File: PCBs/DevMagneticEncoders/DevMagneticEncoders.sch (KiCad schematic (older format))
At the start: 23 parts, among them J1 Conn_01x06_Male, J2 Conn_01x06_Male, J3 Screw_Terminal_01x02, J4 Conn_02x03_Odd_Even, J5 Conn_02x03_Odd_Even, J6 Conn_01x06_Male, J7 Conn_01x04_Male, J8 Conn_01x04_Male, U1 AZ1117-3.3, U2 ESP32-S2-WROOM

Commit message: 5 stepper board
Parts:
- removed J6: Conn_01x06_Male, Connector_JST:JST_PH_B6B-PH-K_1x06_P2.00mm_Vertical, symbol Connector:Conn_01x06_Male
- added A3, A4, A5: Pololu_Breakout_DRV8825, Module:Pololu_Breakout-16_15.2x20.3mm, symbol Driver_Motor:Pololu_Breakout_DRV8825
- added C10: 0.1U, Capacitor_SMD:C_0805_2012Metric_Pad1.18x1.45mm_HandSolder, symbol Device:C
- added C11: 100U, Capacitor_SMD:CP_Elec_6.3x7.7, symbol Device:CP
- added C12, C13, C14: 100u, Capacitor_SMD:CP_Elec_6.3x7.7, symbol Device:CP
- added C15, C16, C17, C7, C8: 0.1u, Capacitor_SMD:C_0805_2012Metric_Pad1.18x1.45mm_HandSolder, symbol Device:C
- added C9: 1U, Capacitor_SMD:C_0805_2012Metric_Pad1.18x1.45mm_HandSolder, symbol Device:C
- added J10, J11, J12: Conn_01x06_Male, Connector_JST:JST_XH_B6B-XH-A_1x06_P2.50mm_Vertical, symbol Connector:Conn_01x06_Male
- added J13, J14, J15: Conn_02x03_Odd_Even, Connector_PinHeader_2.54mm:PinHeader_2x03_P2.54mm_Vertical, symbol Connector_Generic:Conn_02x03_Odd_Even
- added J16, J17, J18: Conn_01x04_Male, Connector_JST:JST_XH_B4B-XH-A_1x04_P2.50mm_Vertical, symbol Connector:Conn_01x04_Male
- added J6: Conn_01x03_Male, Connector_PinHeader_2.54mm:PinHeader_1x03_P2.54mm_Vertical, symbol Connector:Conn_01x03_Male
- added J9: Conn_01x02_Male, Connector_JST:JST_XH_B2B-XH-A_1x02_P2.50mm_Vertical, symbol Connector:Conn_01x02_Male
- added R5: 0.1, Resistor_SMD:R_0805_2012Metric_Pad1.20x1.40mm_HandSolder, symbol Device:R
- added S2: TL3315NF160Q, A4:TL3305AF160QG, symbol dk_Tactile-Switches:TL3315NF160Q
- added U3: ZXBM5210-S, Package_SO:SOIC-8_3.9x4.9mm_P1.27mm, symbol Driver_Motor:ZXBM5210-S
- added U4: TB67H451FNG,EL, Package_SO:SOIC-8-1EP_3.9x4.9mm_P1.27mm_EP2.29x3mm_ThermalVias, symbol BoilerBot:TB67H451FNG,EL
- S1: footprint A4:CK_PTS647_4.5x4.5 -> A4:TL3305AF160QG
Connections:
- net +12V: now also A3.8 (VMOT), A4.8 (VMOT), A5.8 (VMOT), C10.1, C11.1, C12.1, C13.1, C14.1, C15.1, C16.1, C17.1, C7.1, C8.1, U3.2 (VM), U4.5 (VM)
- net +3V3: now also A3.13 (~RST), A3.14 (~SLP), A4.13 (~RST), A4.14 (~SLP), A5.13 (~RST), A5.14 (~SLP), C9.1, J10.1 (Pin_1), J11.1 (Pin_1), J12.1 (Pin_1), J13.1 (Pin_1), J13.3 (Pin_3), J13.5 (Pin_5), J14.1 (Pin_1), J14.3 (Pin_3), J14.5 (Pin_5), J15.1 (Pin_1), J15.3 (Pin_3), J15.5 (Pin_5), U3.3 (VDD)
- net CHARGE: now also U2.16 (IO13); no longer U2.20 (IO17)
- net CLK: now also U2.29 (IO35), J10.3 (Pin_3), J11.3 (Pin_3), J12.3 (Pin_3); no longer U2.25 (IO26)
- net CS0: now also U2.39 (IO45); no longer U2.27 (IO33)
- net CS1: now also U2.36 (IO42); no longer U2.23 (IO20)
- net EN1: now also U2.15 (IO12); no longer U2.6 (IO3)
- net GND: now also A3.1 (GND), A3.7 (GND), A4.1 (GND), A4.7 (GND), A5.1 (GND), A5.7 (GND), C10.2, C11.2, C12.2, C13.2, C14.2, C15.2, C16.2, C17.2, C7.2, C8.2, C9.2, J10.2 (Pin_2), J11.2 (Pin_2), J12.2 (Pin_2), J6.3 (Pin_3), R5.2, S2.4, U3.8 (GND), U4.1 (GND), U4.9 (EP)
- net IO0: now also S2.1
- net MISO: now also U2.34 (IO40), J10.4 (Pin_4), J11.4 (Pin_4), J12.4 (Pin_4); no longer U2.24 (IO21)
- net MOSI: now also U2.31 (IO37), J10.6 (Pin_6), J11.6 (Pin_6), J12.6 (Pin_6); no longer U2.22 (IO19)
- net RX: now also J6.2 (Pin_2)
- net TX: now also J6.1 (Pin_1)
- net EN3: now reaches U2.11 (IO8)
- net EN3: now also A4.9 (~EN)
- net DIR2: now reaches U2.12 (IO9)
- net DIR2: now also A3.16 (DIR)
- net STEP2: now reaches U2.13 (IO10)
- net STEP2: now also A3.15 (STEP)
- net EN2: now reaches U2.14 (IO11)
- net EN2: now also A3.9 (~EN)
- net CS4: now reaches U2.28 (IO34)
- net CS4: now also J12.5 (Pin_5)
- net CS3: now reaches U2.30 (IO36)
- net CS3: now also J11.5 (Pin_5)
- net MOT1: now reaches U2.32 (IO38)
- net MOT1: now also U3.4 (FWD), U4.3 (IN1)
- net MOT2: now reaches U2.33 (IO39)
- net MOT2: now also U3.5 (REV), U4.2 (IN2)
- net CS2: now reaches U2.35 (IO41)
- net CS2: now also J10.5 (Pin_5)
- new net: A5.12 (M2), J15.2 (Pin_2)
- new net: A5.11 (M1), J15.4 (Pin_4)
- new net: A5.10 (M0), J15.6 (Pin_6)
- new net: A5.6 (B2), J18.1 (Pin_1)
- new net: A5.5 (B1), J18.2 (Pin_2)
- new net: A5.4 (A1), J18.3 (Pin_3)
- new net: A5.3 (A2), J18.4 (Pin_4)
- new net: A4.12 (M2), J14.2 (Pin_2)
- new net: A4.11 (M1), J14.4 (Pin_4)
- new net: A4.10 (M0), J14.6 (Pin_6)
- new net: A4.6 (B2), J17.1 (Pin_1)
- new net: A4.5 (B1), J17.2 (Pin_2)
- new net: A4.4 (A1), J17.3 (Pin_3)
- new net: A4.3 (A2), J17.4 (Pin_4)
- new net: A3.12 (M2), J13.2 (Pin_2)
- new net: A3.11 (M1), J13.4 (Pin_4)
- new net: A3.10 (M0), J13.6 (Pin_6)
- new net: A3.6 (B2), J16.1 (Pin_1)
- new net: A3.5 (B1), J16.2 (Pin_2)
- new net: A3.4 (A1), J16.3 (Pin_3)
- new net: A3.3 (A2), J16.4 (Pin_4)
- new net DAC1: U2.20 (IO17), U3.6 (VREF), U4.4 (VREF)
- new net DIR3: A4.16 (DIR), U2.23 (IO20)
- new net DIR4: A5.16 (DIR), U2.27 (IO33)
- new net EN4: A5.9 (~EN), U2.24 (IO21)
- new net OUT1: J9.2 (Pin_2), U3.1 (OUT1), U4.6 (OUT1)
- new net OUT2: J9.1 (Pin_1), U3.7 (OUT2), U4.8 (OUT2)
- new net RS: R5.1, U4.7 (RS)
- new net STEP3: A4.15 (STEP), U2.22 (IO19)
- new net STEP4: A5.15 (STEP), U2.25 (IO26)
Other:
- moved on the sheet: C6, R3, R4

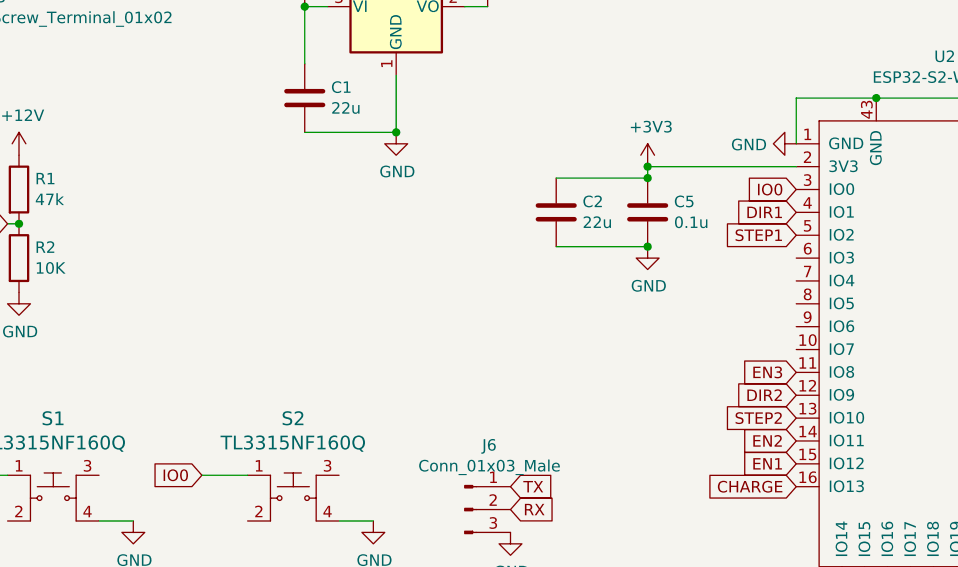
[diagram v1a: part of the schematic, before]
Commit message: added load cell connector
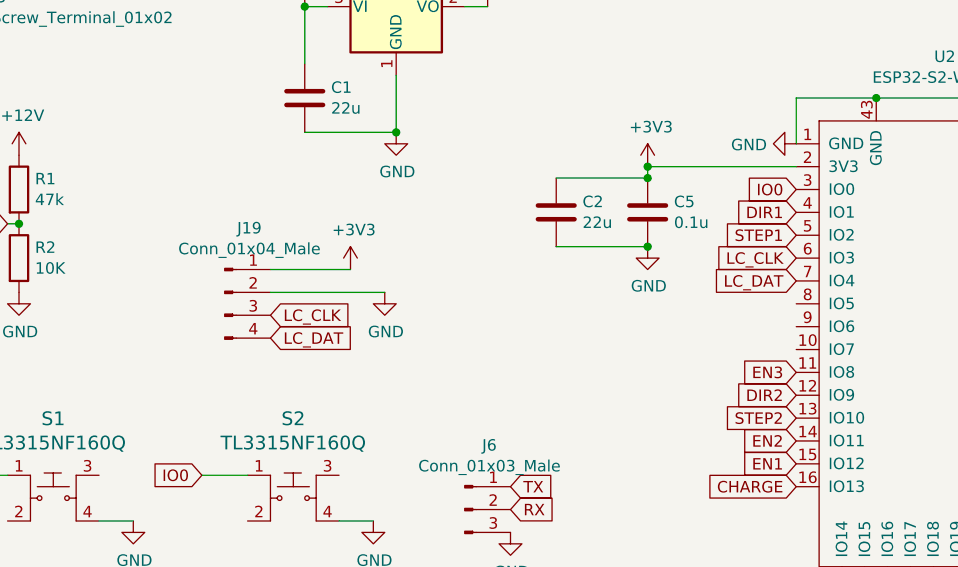
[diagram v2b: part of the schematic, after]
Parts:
- added J19: Conn_01x04_Male, Connector_JST:JST_XH_B4B-XH-A_1x04_P2.50mm_Vertical, symbol Connector:Conn_01x04_Male
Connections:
- net +3V3: now also J19.1 (Pin_1)
- net GND: now also J19.2 (Pin_2)
- net LC_CLK: now reaches U2.6 (IO3)
- net LC_CLK: now also J19.3 (Pin_3)
- net LC_DAT: now reaches U2.7 (IO4)
- net LC_DAT: now also J19.4 (Pin_4)
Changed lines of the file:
@@
 Wire Wire Line
 	6200 1800 6550 1800
+$Comp
+L Connector:Conn_01x04_Male J19
+U 1 1 6113B222
+P 2400 2350
+AR Path="/6113B222" Ref="J19"  Part="1"
+AR Path="/6090A275/6113B222" Ref="J?"  Part="1"
+AR Path="/60A3186D/6090A275/6113B222" Ref="J?"  Part="1"
+F 0 "J19" H 2508 2631 50  0000 C CNN
+F 1 "Conn_01x04_Male" H 2508 2540 50  0000 C CNN
+F 2 "Connector_JST:JST_XH_B4B-XH-A_1x04_P2.50mm_Vertical" H 2400 2350 50  0001 C CNN
+F 3 "~" H 2400 2350 50  0001 C CNN
+	1    2400 2350
+	1    0    0    -1
+$EndComp
+$Comp
+L power:+3V3 #PWR?
+U 1 1 6113C85F
+P 2950 2250
+AR Path="/60A3186D/6113C85F" Ref="#PWR?"  Part="1"
+AR Path="/6113C85F" Ref="#PWR060"  Part="1"
+F 0 "#PWR060" H 2950 2100 50  0001 C CNN
+F 1 "+3V3" H 2965 2423 50  0000 C CNN
+F 2 "" H 2950 2250 50  0001 C CNN
+F 3 "" H 2950 2250 50  0001 C CNN
+	1    2950 2250
+	1    0    0    -1
+$EndComp
+$Comp
+L power:GND #PWR?
+U 1 1 6113D113
+P 3100 2350
+AR Path="/60A3186D/6113D113" Ref="#PWR?"  Part="1"
+AR Path="/6113D113" Ref="#PWR061"  Part="1"
+F 0 "#PWR061" H 3100 2100 50  0001 C CNN
+F 1 "GND" H 3105 2177 50  0000 C CNN
+F 2 "" H 3100 2350 50  0001 C CNN
+F 3 "" H 3100 2350 50  0001 C CNN
+	1    3100 2350
+	1    0    0    -1
+$EndComp
+Text GLabel 4900 2200 0    50   Input ~ 0
+LC_CLK
+Text GLabel 4900 2300 0    50   Input ~ 0
+LC_DAT
+Text GLabel 2600 2450 2    50   Input ~ 0
+LC_CLK
+Text GLabel 2600 2550 2    50   Input ~ 0
+LC_DAT
+Wire Wire Line
+	2600 2250 2950 2250
+Wire Wire Line
+	3100 2350 2600 2350
 $EndSCHEMATC
